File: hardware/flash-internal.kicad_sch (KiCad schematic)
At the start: 4 parts, among them U8 SST39SF010A-55-4I-WHE, U9 SST39SF010A-55-4I-WHE

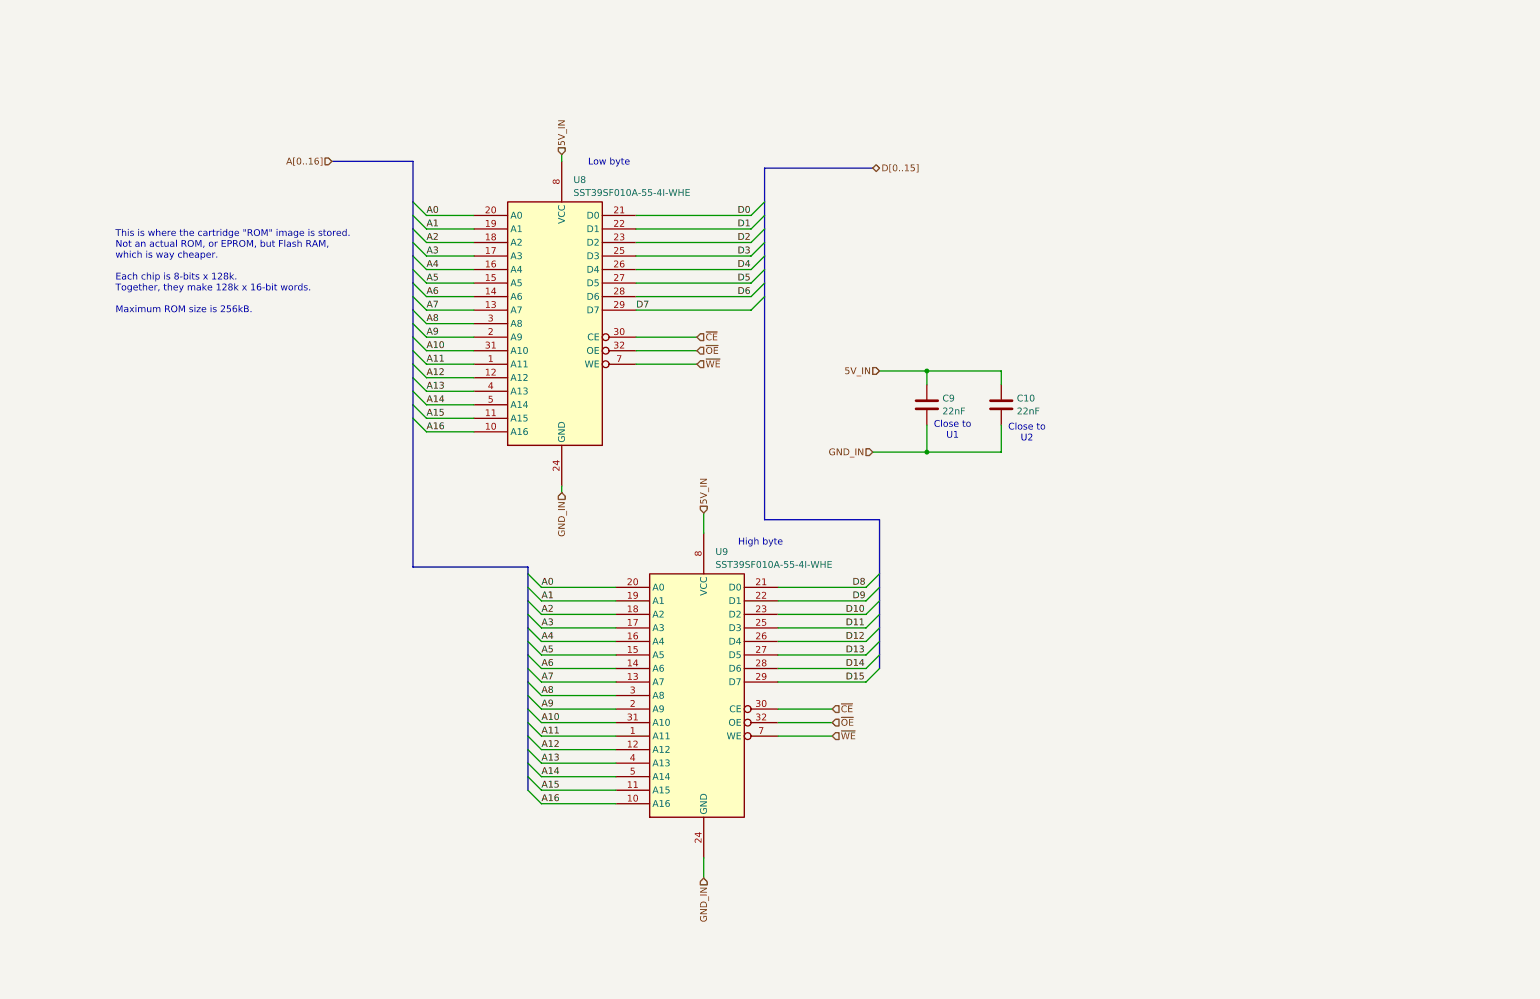
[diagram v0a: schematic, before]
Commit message: Massively reorganize board designs
Now planning to have most assembly done by JLCPCB, so trace sizes,
part selections, etc. are set accordingly.

New boards are:
 - cartridge interface & flash
 - microcontroller & registers
 - sram x2
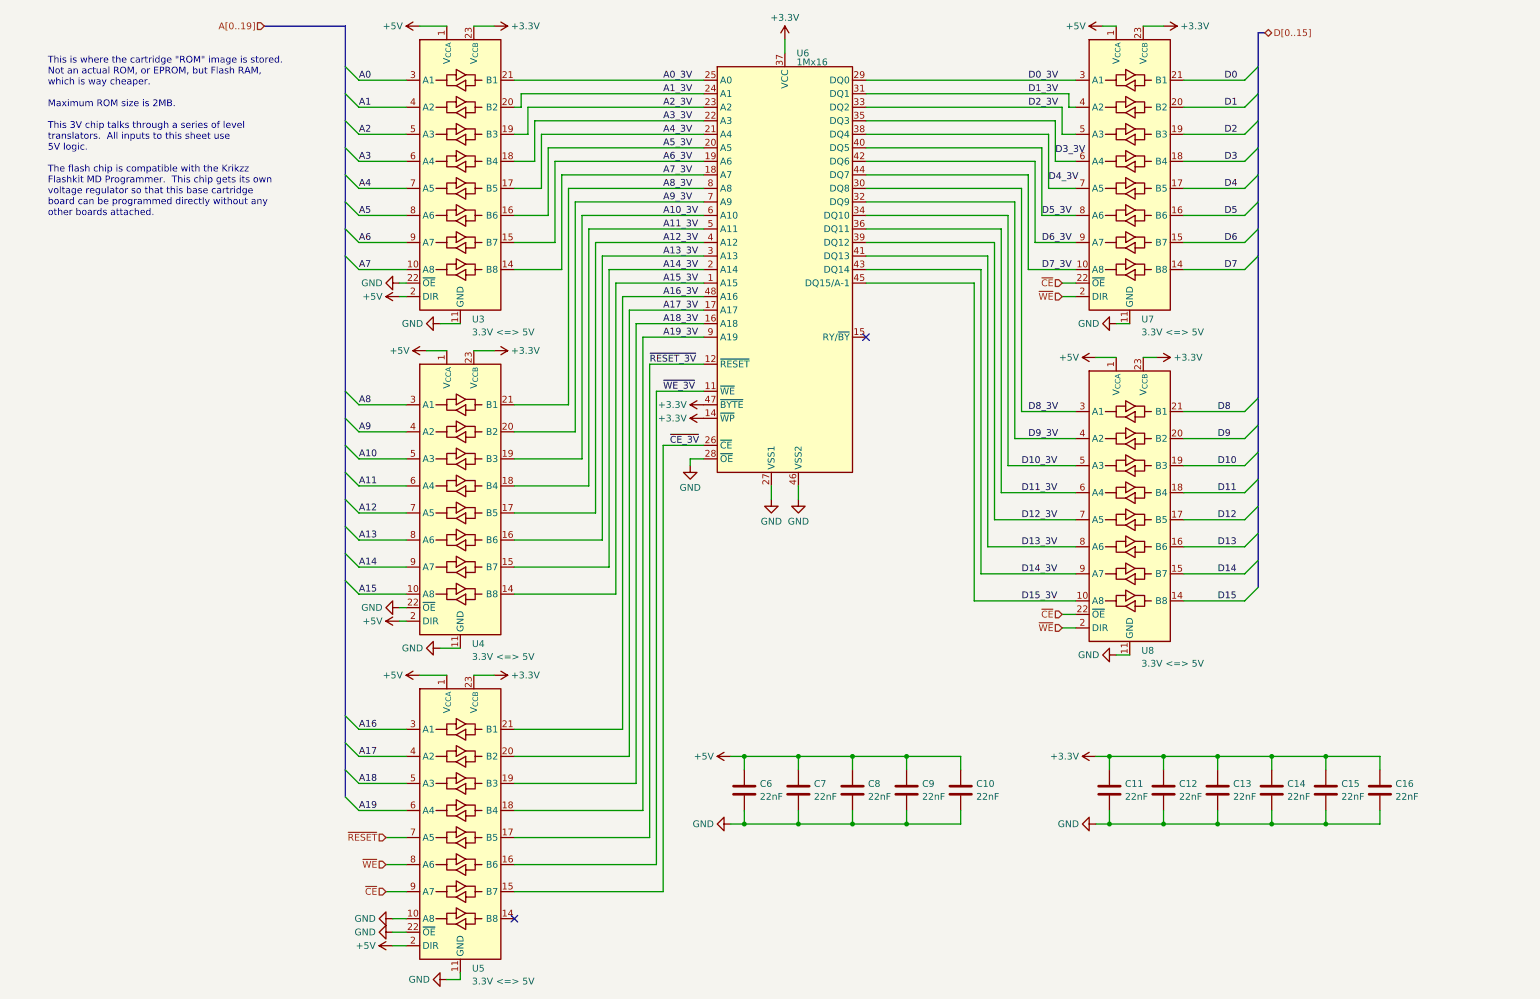
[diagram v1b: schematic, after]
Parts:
- removed U8, U9: SST39SF010A-55-4I-WHE, Package_SO:TSOP-I-32_14.4x8mm_P0.5mm, symbol Memory_Flash:29F010-TSOP-SP
- added C10, C11, C12, C13, C14, C15, C16, C8, C9: 22nF, Capacitor_SMD:C_0603_1608Metric, symbol Device:C
- added U3, U4, U5, U7, U8: 3.3V <=> 5V, Package_SO:SSOP-24_5.3x8.2mm_P0.65mm, symbol Logic_LevelTranslator:SN74LVC8T245
- added U6: 1Mx16, Package_SO:TSOP-I-48_18.4x12mm_P0.5mm, symbol S29AL016J55TFIR20:S29AL016J55TFIR20
- C6: renamed from C9; JLCPCB Part Number (none) -> CL10B223KB8NNNC; Mouser Part Number (none) -> 80-C0603C223K4R; Part Number (none) -> C0603C223K4RACTU
- C7: renamed from C10; JLCPCB Part Number (none) -> CL10B223KB8NNNC; Mouser Part Number (none) -> 80-C0603C223K4R; Part Number (none) -> C0603C223K4RACTU
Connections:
- net A0: now also U3.3 (A1)
- net A1: now also U3.4 (A2)
- net A10: now also U4.5 (A3)
- net A11: now also U4.6 (A4)
- net A12: now also U4.7 (A5)
- net A13: now also U4.8 (A6)
- net A14: now also U4.9 (A7)
- net A15: now also U4.10 (A8)
- net A16: now also U5.3 (A1)
- net A2: now also U3.5 (A3)
- net A3: now also U3.6 (A4)
- net A4: now also U3.7 (A5)
- net A5: now also U3.8 (A6)
- net A6: now also U3.9 (A7)
- net A7: now also U3.10 (A8)
- net A8: now also U4.3 (A1)
- net A9: now also U4.4 (A2)
- net D0: now also U7.21 (B1)
- net D1: now also U7.20 (B2)
- net D10: now also U8.19 (B3)
- net D11: now also U8.18 (B4)
- net D12: now also U8.17 (B5)
- net D13: now also U8.16 (B6)
- net D14: now also U8.15 (B7)
- net D15: now also U8.14 (B8)
- net D2: now also U7.19 (B3)
- net D3: now also U7.18 (B4)
- net D4: now also U7.17 (B5)
- net D5: now also U7.16 (B6)
- net D6: now also U7.15 (B7)
- net D7: now also U7.14 (B8)
- net D8: now also U8.21 (B1)
- net D9: now also U8.20 (B2)
- net ~{CE}: now also U5.9 (A7), U7.22 (~{OE}), U8.22 (~{OE})
- net ~{WE}: now also U5.8 (A6), U7.2 (DIR), U8.2 (DIR)
- net 5V_IN renamed +5V
- net +5V: now also C10.1, C8.1, C9.1, U3.1 (V_{CCA}), U3.2 (DIR), U4.1 (V_{CCA}), U4.2 (DIR), U5.1 (V_{CCA}), U5.2 (DIR), U7.1 (V_{CCA}), U8.1 (V_{CCA})
- net GND_IN renamed GND
- net GND: now also C10.2, C11.2, C12.2, C13.2, C14.2, C15.2, C16.2, C8.2, C9.2, U3.11 (GND), U3.12 (GND), U3.13 (GND), U3.22 (~{OE}), U4.11 (GND), U4.12 (GND), U4.13 (GND), U4.22 (~{OE}), U5.10 (A8), U5.11 (GND), U5.12 (GND), U5.13 (GND), U5.22 (~{OE}), U6.27 (VSS1), U6.28 (~{OE}), U6.46 (VSS2), U7.11 (GND), U7.12 (GND), U7.13 (GND), U8.11 (GND), U8.12 (GND), U8.13 (GND)
- new net +3.3V: C11.1, C12.1, C13.1, C14.1, C15.1, C16.1, U3.23 (V_{CCB}), U3.24 (V_{CCB}), U4.23 (V_{CCB}), U4.24 (V_{CCB}), U5.23 (V_{CCB}), U5.24 (V_{CCB}), U6.14 (~{WP}), U6.37 (VCC), U6.47 (~{BYTE}), U7.23 (V_{CCB}), U7.24 (V_{CCB}), U8.23 (V_{CCB}), U8.24 (V_{CCB})
- new net A0_3V: U3.21 (B1), U6.25 (A0)
- new net A10_3V: U4.19 (B3), U6.6 (A10)
- new net A11_3V: U4.18 (B4), U6.5 (A11)
- new net A12_3V: U4.17 (B5), U6.4 (A12)
- new net A13_3V: U4.16 (B6), U6.3 (A13)
- new net A14_3V: U4.15 (B7), U6.2 (A14)
- new net A15_3V: U4.14 (B8), U6.1 (A15)
- new net A16_3V: U5.21 (B1), U6.48 (A16)
- new net A17: U5.4 (A2)
- new net A17_3V: U5.20 (B2), U6.17 (A17)
- new net A18: U5.5 (A3)
- new net A18_3V: U5.19 (B3), U6.16 (A18)
- new net A19: U5.6 (A4)
- new net A19_3V: U5.18 (B4), U6.9 (A19)
- new net A1_3V: U3.20 (B2), U6.24 (A1)
- new net A2_3V: U3.19 (B3), U6.23 (A2)
- new net A3_3V: U3.18 (B4), U6.22 (A3)
- new net A4_3V: U3.17 (B5), U6.21 (A4)
- new net A5_3V: U3.16 (B6), U6.20 (A5)
- new net A6_3V: U3.15 (B7), U6.19 (A6)
- new net A7_3V: U3.14 (B8), U6.18 (A7)
- new net A8_3V: U4.21 (B1), U6.8 (A8)
- new net A9_3V: U4.20 (B2), U6.7 (A9)
- new net D0_3V: U6.29 (DQ0), U7.3 (A1)
- new net D10_3V: U6.34 (DQ10), U8.5 (A3)
- new net D11_3V: U6.36 (DQ11), U8.6 (A4)
- new net D12_3V: U6.39 (DQ12), U8.7 (A5)
- new net D13_3V: U6.41 (DQ13), U8.8 (A6)
- new net D14_3V: U6.43 (DQ14), U8.9 (A7)
- new net D15_3V: U6.45 (DQ15/A-1), U8.10 (A8)
- new net D1_3V: U6.31 (DQ1), U7.4 (A2)
- new net D2_3V: U6.33 (DQ2), U7.5 (A3)
- new net D3_3V: U6.35 (DQ3), U7.6 (A4)
- new net D4_3V: U6.38 (DQ4), U7.7 (A5)
- new net D5_3V: U6.40 (DQ5), U7.8 (A6)
- new net D6_3V: U6.42 (DQ6), U7.9 (A7)
- new net D7_3V: U6.44 (DQ7), U7.10 (A8)
- new net D8_3V: U6.30 (DQ8), U8.3 (A1)
- new net D9_3V: U6.32 (DQ9), U8.4 (A2)
- new net ~{CE_3V}: U5.15 (B7), U6.26 (~{CE})
- new net ~{RESET_3V}: U5.17 (B5), U6.12 (~{RESET})
- new net ~{RESET}: U5.7 (A5)
- new net ~{WE_3V}: U5.16 (B6), U6.11 (~{WE})
- no-connect marks 0 -> 2
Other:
- note added: "This is where the cartridge "ROM" image is stored. Not an actual ROM, or EPROM, but Flash RAM, which is way cheaper. Maximum ROM size is 2MB. This 3V chip talks through a series of level translators. All inputs to this sheet use 5V logic. The flash chip is compatible with the Krikzz Flashkit MD Programmer. This chip gets its own voltage regulator so that this base cartridge board can be programme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"
- note removed: "Close to U1"
- note removed: "Close to U2"
- note removed: "High byte"
- note removed: "Low byte"
- note removed: "This is where the cartridge "ROM" image is stored. Not an actual ROM, or EPROM, but Flash RAM, which is way cheaper. Each chip is 8-bits x 128k. Together, they make 128k x 16-bit words. Maximum ROM size is 256kB."
- title: Kinetoscope Flash connected to buses -> Kinetoscope Flash chip and related support circuits
- moved on the sheet: C6, C7

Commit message: Redo cart board
The first cartridge board I ordered did not work.  💰🚽

Problems I ran into:
 - The FlashKit Programmer sends 3.3V logic, not 5V logic like the
   Sega
 - I had one hard-coded input to my address decoder inverted
 - One pair of level translators had their supply voltages backward
 - I had hard-coded #OE on the flash chip, but #OE and #WE are
   mutually exclusive on this particular chip

Changes:
 - Add debug connectors (not populated by default) for power and flash
   control signals
 - Fix flash ~OE signal, which is mutually exclusive with ~WE
 - Fix level translators for compatibility with both 3.3V and 5V logic
 - Replace decoder with a smaller, simpler one with no latches and
   5V-tolerance
 - Reorient translators to simplify traces
 - Increase trace width for supply traces
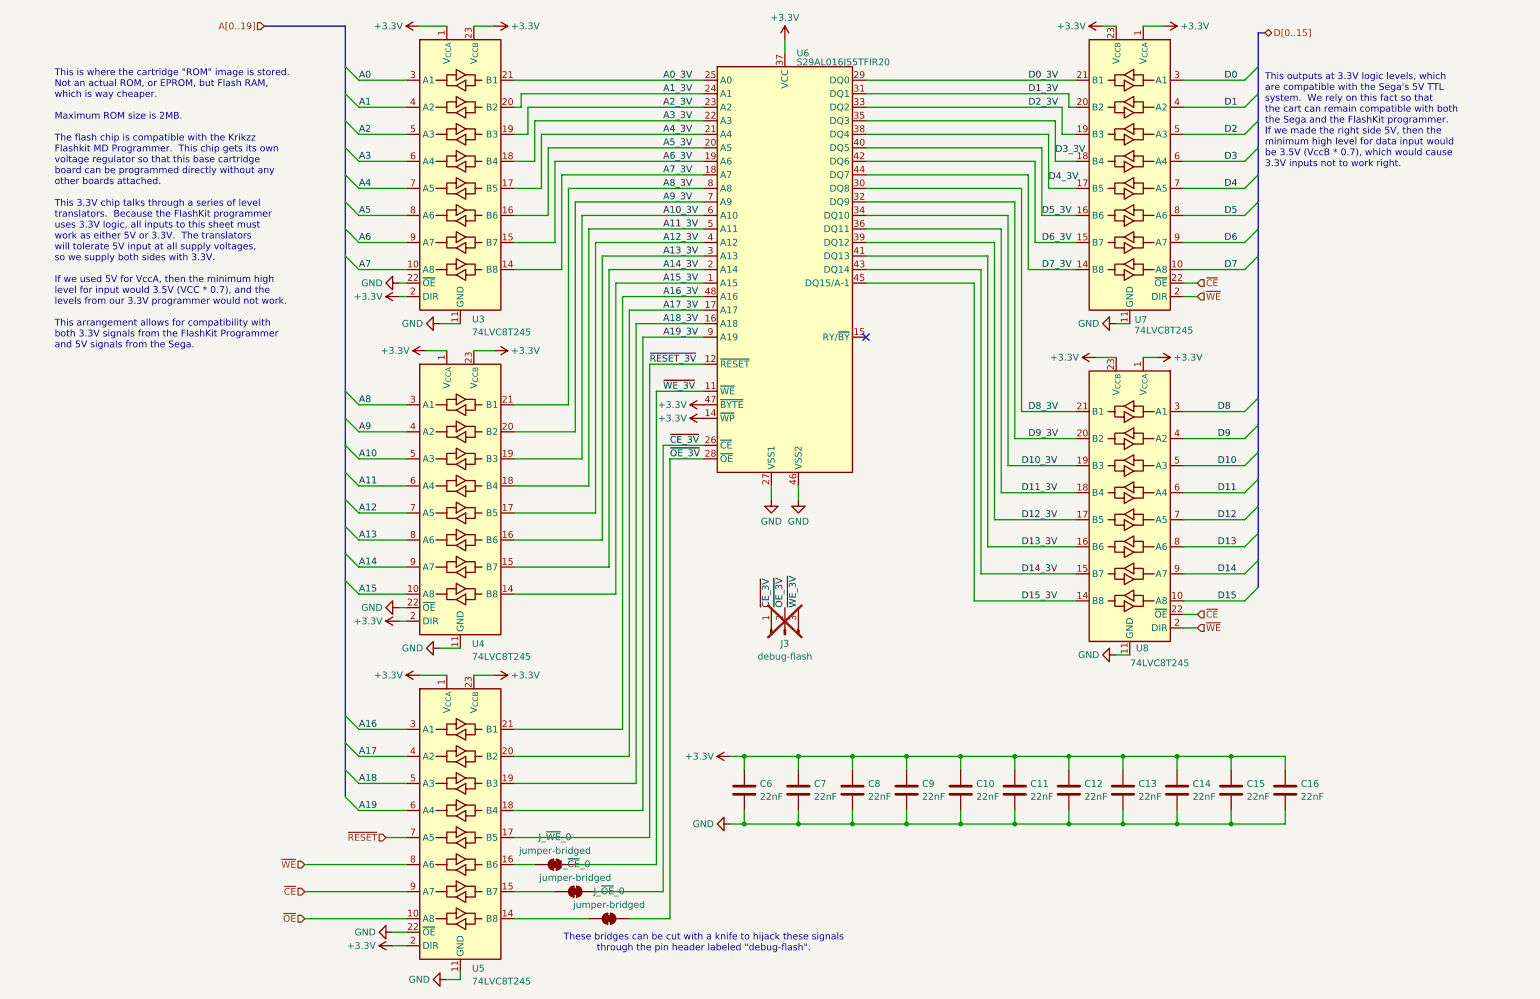
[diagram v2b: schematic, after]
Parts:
- added J3: debug-flash, Connector_PinHeader_2.54mm:PinHeader_1x03_P2.54mm_Horizontal, symbol Connector:Conn_01x03_Pin
- added J_~{CE}_0, J_~{OE}_0, J_~{WE}_0: jumper-bridged, Jumper:SolderJumper-2_P1.3mm_Bridged_RoundedPad1.0x1.5mm, symbol Jumper:SolderJumper_2_Bridged
- U3, U4, U5, U7, U8: value 3.3V <=> 5V -> 74LVC8T245
- U6: value 1Mx16 -> S29AL016J55TFIR20
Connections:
- net +5V is gone; now on net +3.3V: C10.1, C6.1, C7.1, C8.1, C9.1, U3.1 (V_{CCA}), U3.2 (DIR), U4.1 (V_{CCA}), U4.2 (DIR), U5.1 (V_{CCA}), U5.2 (DIR), U7.1 (V_{CCA}), U8.1 (V_{CCA})
- net D0: now also U7.3 (A1); no longer U7.21 (B1)
- net D0_3V: now also U7.21 (B1); no longer U7.3 (A1)
- net D1: now also U7.4 (A2); no longer U7.20 (B2)
- net D10: now also U8.5 (A3); no longer U8.19 (B3)
- net D10_3V: now also U8.19 (B3); no longer U8.5 (A3)
- net D11: now also U8.6 (A4); no longer U8.18 (B4)
- net D11_3V: now also U8.18 (B4); no longer U8.6 (A4)
- net D12: now also U8.7 (A5); no longer U8.17 (B5)
- net D12_3V: now also U8.17 (B5); no longer U8.7 (A5)
- net D13: now also U8.8 (A6); no longer U8.16 (B6)
- net D13_3V: now also U8.16 (B6); no longer U8.8 (A6)
- net D14: now also U8.9 (A7); no longer U8.15 (B7)
- net D14_3V: now also U8.15 (B7); no longer U8.9 (A7)
- net D15: now also U8.10 (A8); no longer U8.14 (B8)
- net D15_3V: now also U8.14 (B8); no longer U8.10 (A8)
- net D1_3V: now also U7.20 (B2); no longer U7.4 (A2)
- net D2: now also U7.5 (A3); no longer U7.19 (B3)
- net D2_3V: now also U7.19 (B3); no longer U7.5 (A3)
- net D3: now also U7.6 (A4); no longer U7.18 (B4)
- net D3_3V: now also U7.18 (B4); no longer U7.6 (A4)
- net D4: now also U7.7 (A5); no longer U7.17 (B5)
- net D4_3V: now also U7.17 (B5); no longer U7.7 (A5)
- net D5: now also U7.8 (A6); no longer U7.16 (B6)
- net D5_3V: now also U7.16 (B6); no longer U7.8 (A6)
- net D6: now also U7.9 (A7); no longer U7.15 (B7)
- net D6_3V: now also U7.15 (B7); no longer U7.9 (A7)
- net D7: now also U7.10 (A8); no longer U7.14 (B8)
- net D7_3V: now also U7.14 (B8); no longer U7.10 (A8)
- net D8: now also U8.3 (A1); no longer U8.21 (B1)
- net D8_3V: now also U8.21 (B1); no longer U8.3 (A1)
- net D9: now also U8.4 (A2); no longer U8.20 (B2)
- net D9_3V: now also U8.20 (B2); no longer U8.4 (A2)
- net GND: no longer U5.10 (A8), U6.28 (~{OE})
- net ~{CE_3V}: now also J3.1 (Pin_1), J_~{CE}_0.2 (B); no longer U5.15 (B7)
- net ~{WE_3V}: now also J3.3 (Pin_3), J_~{WE}_0.2 (B); no longer U5.16 (B6)
- net at U5.14 (B8): now also J_~{OE}_0.1 (A)
- new net: J_~{WE}_0.1 (A), U5.16 (B6)
- new net: J_~{CE}_0.1 (A), U5.15 (B7)
- new net ~{OE_3V}: J3.2 (Pin_2), J_~{OE}_0.2 (B), U6.28 (~{OE})
- new net ~{OE}: U5.10 (A8)
- no-connect marks 2 -> 1
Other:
- note added: "These bridges can be cut with a knife to hijack these signals through the pin header labeled "debug-flash"."
- note added: "This is where the cartridge "ROM" image is stored. Not an actual ROM, or EPROM, but Flash RAM, which is way cheaper. Maximum ROM size is 2MB. The flash chip is compatible with the Krikzz Flashkit MD Programmer. This chip gets its own voltage regulator so that this base cartridge board can be programmed directly without any other boards attached. This 3.3V chip talks through a series of level tran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"
- note added: "This outputs at 3.3V logic levels, which are compatible with the Sega's 5V TTL system. We rely on this fact so that the cart can remain compatible with both the Sega and the FlashKit programmer. If we made the right side 5V, then the minimum high level for data input would be 3.5V (VccB * 0.7), which would cause 3.3V inputs not to work right."
- note removed: "This is where the cartridge "ROM" image is stored. Not an actual ROM, or EPROM, but Flash RAM, which is way cheaper. Maximum ROM size is 2MB. This 3V chip talks through a series of level translators. All inputs to this sheet use 5V logic. The flash chip is compatible with the Krikzz Flashkit MD Programmer. This chip gets its own voltage regulator so that this base cartridge board can be programme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"
- moved on the sheet: C11, C12, C13, C14, C15, C16
